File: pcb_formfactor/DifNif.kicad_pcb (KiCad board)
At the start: 2 copper layers, 98.8 x 93 mm, 85 parts, among them J1 DBA-ESDI, J2 PROG, J3 SDCARD_DM3AT-SF-PEJM5, J4 HPLA_PORT, U1 ICE40HX4K-TQ144, U10 74LVC4245, U11 74LCX07, U12 74VHCT125, U13 Teensy4_1, U14 74LVC4245, U2 SST26VF080A-104I/SN, U3 APX803S00-29SA-7, U4 AP2114HA-3.3, U5 AP2114HA-1.2, U6 74LVC4245, U7 74LVC4245, U8 74LVC4245, U9 74LVC4245, X1 ASE-xxxMHz

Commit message: Rev P2: update PCB from schematic
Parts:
- U10, U14, U6, U7, U8, U9: value 74LVC4245 -> 74LVC8T245
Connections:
- J1 pad b14: /DifNifBus/~{CHRESET}_5V -> /DifNifBus/CHRESET_5V
- J1 pad b8: unconnected-(J1-Padb8) -> /DifNifBus/~{CD_SFDBK}_5V
- J4 pad 10: unconnected-(J4-Pad10) -> /~{CD_DS16}
- J4 pad 11: unconnected-(J4-Pad11) -> /~{CD_SFDBK}
- J4 pad 12: unconnected-(J4-Pad12) -> /DATA_DIR
- J4 pad 13: unconnected-(J4-Pad13) -> /ARB/~{GNT}
- J4 pad 14: unconnected-(J4-Pad14) -> /~{PREEMPT}
- J4 pad 4: unconnected-(J4-Pad4) -> /~{CMD}
- J4 pad 5: unconnected-(J4-Pad5) -> /S0
- J4 pad 6: unconnected-(J4-Pad6) -> /S1
- J4 pad 7: unconnected-(J4-Pad7) -> /M/~{IO}
- J4 pad 8: unconnected-(J4-Pad8) -> /~{CD_SETUP}
- J4 pad 9: unconnected-(J4-Pad9) -> /CHRESET
- U1 pad 134: unconnected-(U1-Pad134) -> /~{CD_SFDBK}
- U12 pad 11: unconnected-(U12-Pad11) -> /DifNifBus/~{CD_SFDBK}_5V
- U12 pad 13: GND -> /~{CD_SFDBK}
- U8 pad 14: /DifNifBus/~{CHRESET}_5V -> /DifNifBus/CHRESET_5V
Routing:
- net /DifNifBus/~{CHRESET}_5V: track 27.4 -> 0.00 mm, vias 3 -> 0
- net /DifNifBus/CHRESET_5V: track 0.00 -> 27.4 mm, vias 0 -> 3

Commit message: Rev P2 layout: route -CD SFDBK via J4 (in progress)
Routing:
- net /~{CD_SFDBK}: track 0.00 -> 62.4 mm, vias 0 -> 7
- net /DifNifBus/~{CD_SFDBK}_5V: track 0.00 -> 59.4 mm, vias 0 -> 3
- net /DifNifBus/CHRESET_5V: track 27.4 -> 29.1 mm

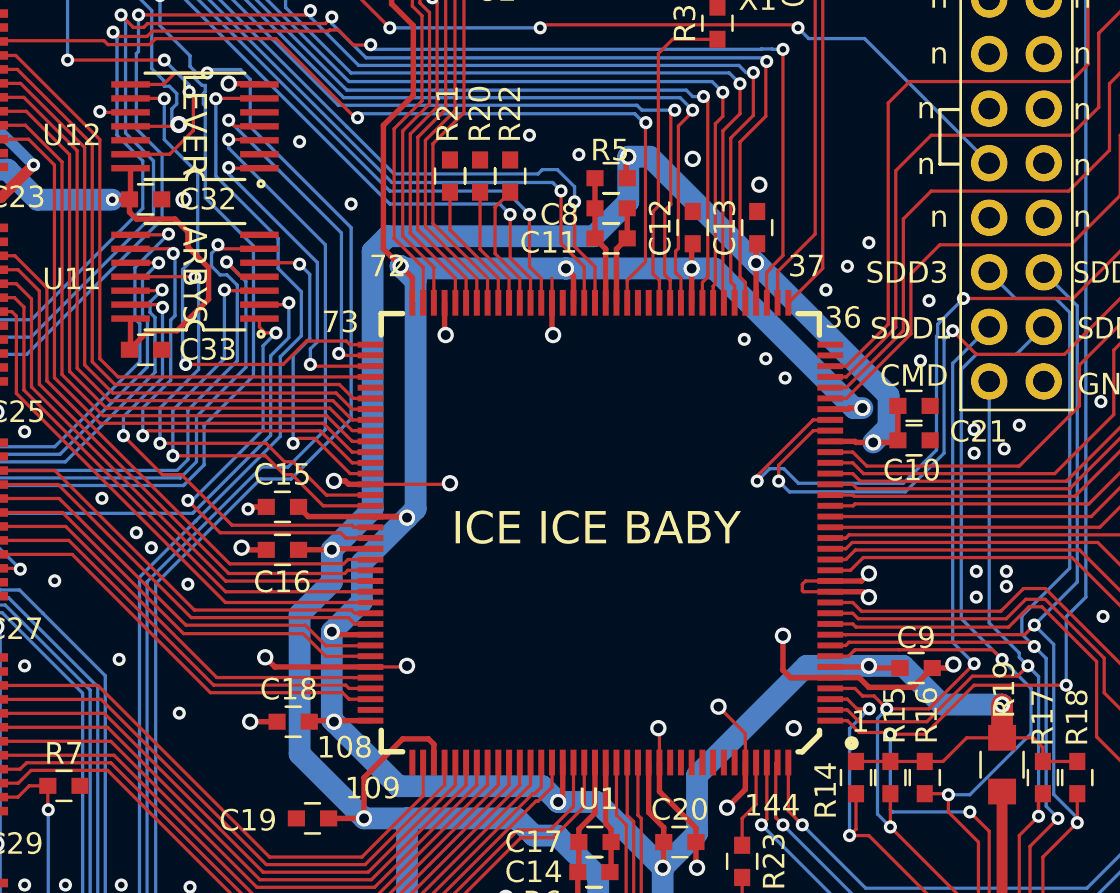
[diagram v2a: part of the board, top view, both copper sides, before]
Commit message: Rev P2 layout: route -CD SFDBK push-pull via J4, reset fix
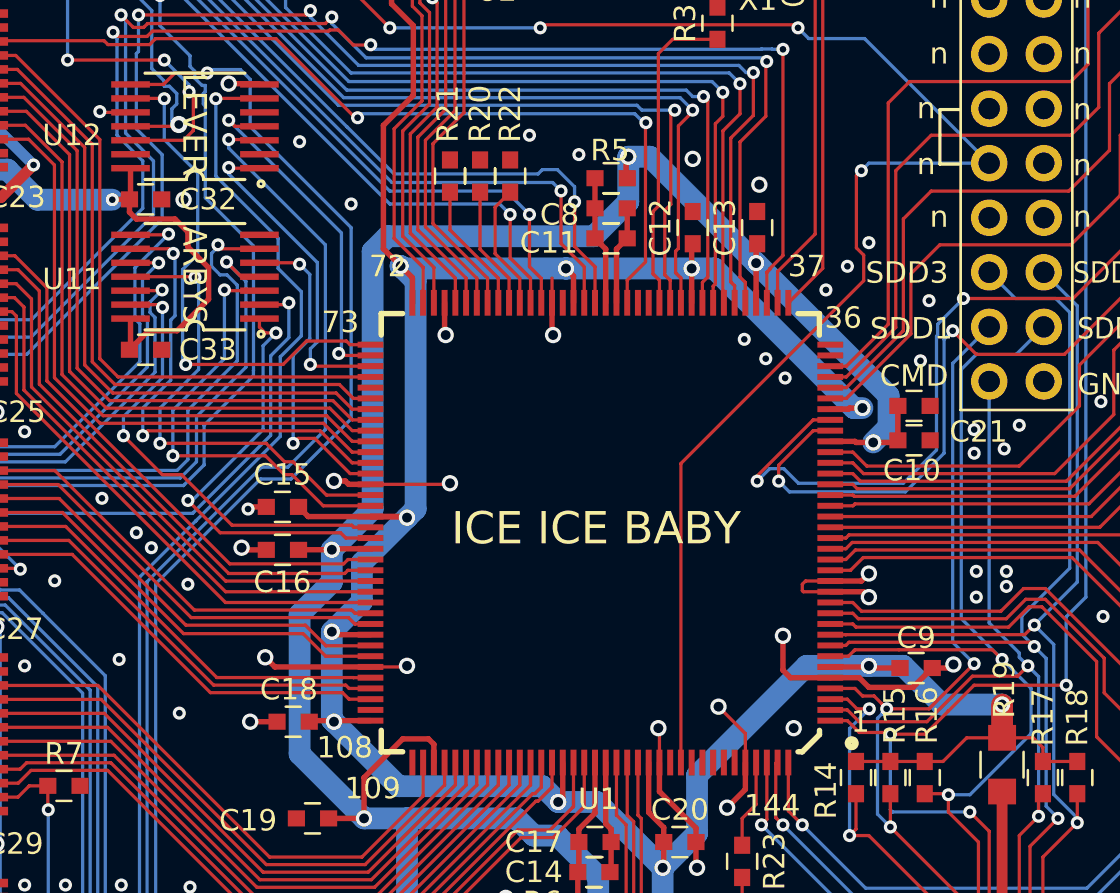
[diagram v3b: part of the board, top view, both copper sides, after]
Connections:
- U12 pad 12: GND -> /~{CD_SFDBK}
- U12 pad 13: /~{CD_SFDBK} -> GND
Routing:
- net /~{CD_SFDBK}: track 62.4 -> 99.5 mm, vias 7 -> 8
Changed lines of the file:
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@@
 			(size 1.8 0.3)
 			(layers "F.Cu" "F.Mask" "F.Paste")
-			(net 2 "GND")
+			(net 86 "/~{CD_SFDBK}")
 			(pintype "input")
 		)
@@
 			(size 1.8 0.3)
 			(layers "F.Cu" "F.Mask" "F.Paste")
-			(net 86 "/~{CD_SFDBK}")
+			(net 2 "GND")
 			(pintype "input")
 		)
@@
 	)
 	(segment
-		(start 121.93 66.885)
-		(end 123.748906 66.885)
+		(start 124.398906 66.235)
+		(end 124.8534 65.780506)
+		(width 0.1524)
+		(layer "F.Cu")
+		(net 86)
+	)
+	(segment
+		(start 124.8534 64.173911)
+		(end 124.657312 63.977823)
 		(width 0.1524)
 		(layer "F.Cu")
@@
 	)
 	(segment
-		(start 123.748906 66.885)
-		(end 124.8534 65.780506)
+		(start 147.55 95.2)
+		(end 147.55 81.28)
+		(width 0.1524)
+		(layer "F.Cu")
+		(net 86)
+	)
+	(segment
+		(start 147.55 81.28)
+		(end 156.058927 72.771073)
+		(width 0.1524)
+		(layer "F.Cu")
+		(net 86)
+	)
+	(segment
+		(start 156.058927 72.771073)
+		(end 156.058927 71.582)
 		(width 0.1524)
 		(layer "F.Cu")
@@
 	)
 	(segment
+		(start 156.058927 71.582)
+		(end 155.718 71.241073)
+		(width 0.1524)
+		(layer "F.Cu")
+		(net 86)
+	)
+	(segment
+		(start 155.718 67.882)
+		(end 155.95 67.65)
+		(width 0.1524)
+		(layer "F.Cu")
+		(net 86)
+	)
+	(segment
 		(start 124.8534 65.780506)
 		(end 124.8534 64.173911)
@@
 	)
 	(segment
-		(start 124.8534 64.173911)
-		(end 124.657312 63.977823)
+		(start 121.93 66.235)
+		(end 124.398906 66.235)
+		(width 0.1524)
+		(layer "F.Cu")
+		(net 86)
+	)
+	(segment
+		(start 155.718 71.241073)
+		(end 155.718 67.882)
 		(width 0.1524)
 		(layer "F.Cu")
@@
 	)
 	(via
+		(at 155.95 67.65)
+		(size 0.6096)
+		(drill 0.3048)
+		(layers "F.Cu" "B.Cu")
+		(net 86)
+	)
+	(via
 		(at 119 58.5)
 		(size 0.6096)
@@
 	)
 	(segment
+		(start 155.95 67.65)
+		(end 156.3 67.3)
+		(width 0.1524)
+		(layer "B.Cu")
+		(net 86)
+	)
+	(segment
 		(start 119 62.5)
 		(end 119 58.5)
@@
 		(width 0.1524)
 		(layer "B.Cu")
+		(net 86)
+	)
+	(segment
+		(start 156.3 67.3)
+		(end 161.9 67.3)
+		(width 0.1524)
+		(layer "B.Cu")
